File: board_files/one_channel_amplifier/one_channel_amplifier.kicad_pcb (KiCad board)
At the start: 2 copper layers, 78.7 x 33.8 mm, 27 parts, among them J1 Screw_Terminal_01x02, J2 Screw_Terminal_01x02, J3 Screw_Terminal_01x02, J4 Conn_01x02, J5 Conn_01x02, J6 Screw_Terminal_01x02, U1 LM3886

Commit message: Finished first rev
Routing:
- added copper zone on B.Cu, net GND
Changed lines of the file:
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@@
     (polygon
       (pts
-        (xy 147.32 84.582) (xy 146.304 84.963) (xy 143.256 95.25) (xy 143.256 98.806) (xy 150.114 98.806)
+        (xy 147.32 84.582) (xy 146.431 84.963) (xy 143.256 95.25) (xy 143.256 98.806) (xy 150.114 98.806)
         (xy 150.114 97.282) (xy 148.209 84.963)
-      )
-    )
-  )
-  (zone (net 2) (net_name VCC) (layer F.Cu) (hatch edge 0.508)
-    (connect_pads yes (clearance 0.508))
-    (min_thickness 0.254)
-    (fill (arc_segments 32) (thermal_gap 0.508) (thermal_bridge_width 0.508) (smoothing fillet) (radius 0.254))
-    (polygon
-      (pts
-        (xy 150.622 86.741) (xy 151.384 86.487) (xy 151.638 86.106) (xy 151.765 85.471) (xy 151.511 84.963)
-        (xy 149.86 82.042) (xy 142.24 82.042) (xy 141.859 84.963) (xy 138.938 86.106) (xy 132.842 92.202)
-        (xy 126.492 97.282) (xy 121.158 101.346) (xy 100.076 101.346) (xy 100.076 109.474) (xy 127 109.474)
-        (xy 138.176 95.758) (xy 145.034 86.868) (xy 145.796 84.328) (xy 148.844 84.328) (xy 149.733 86.233)
-        (xy 150.114 86.614)
-      )
-    )
-  )
-  (zone (net 3) (net_name VEE) (layer F.Cu) (hatch edge 0.508)
-    (priority 4)
-    (connect_pads yes (clearance 0.508))
-    (min_thickness 0.254)
-    (fill (arc_segments 32) (thermal_gap 0.508) (thermal_bridge_width 0.508) (smoothing fillet) (radius 0.254))
-    (polygon
-      (pts
-        (xy 149.987 80.01) (xy 150.114 80.518) (xy 149.987 81.026) (xy 149.606 81.407) (xy 149.098 81.661)
-        (xy 148.844 81.661) (xy 148.336 81.407) (xy 146.431 79.248) (xy 144.78 79.248) (xy 141.732 80.518)
-        (xy 138.684 80.518) (xy 135.382 81.788) (xy 131.572 81.788) (xy 121.92 84.836) (xy 100.076 84.836)
-        (xy 100.076 76.708) (xy 147.066 76.708)
       )
     )
@@
       )
     )
+  )
+  (zone (net 3) (net_name VEE) (layer F.Cu) (hatch edge 0.508)
+    (priority 4)
+    (connect_pads yes (clearance 0.508))
+    (min_thickness 0.254)
+    (fill yes (arc_segments 32) (thermal_gap 0.508) (thermal_bridge_width 0.508) (smoothing fillet) (radius 0.254))
+    (polygon
+      (pts
+        (xy 149.225 81.5975) (xy 149.6695 81.407) (xy 149.987001 81.026) (xy 150.114 80.4545) (xy 149.86 79.8195)
+        (xy 147.5105 76.7715) (xy 99.568 76.708) (xy 99.568 84.836) (xy 122.047 84.836) (xy 131.826 82.6135)
+        (xy 134.366 81.788) (xy 138.684 80.518) (xy 141.732 80.518) (xy 144.78 79.121) (xy 146.431 79.121)
+        (xy 148.1455 81.2165) (xy 148.6535 81.5975)
+      )
+    )
+  )
+  (zone (net 2) (net_name VCC) (layer F.Cu) (hatch edge 0.508)
+    (priority 4)
+    (connect_pads yes (clearance 0.508))
+    (min_thickness 0.254)
+    (fill yes (arc_segments 32) (thermal_gap 0.508) (thermal_bridge_width 0.508) (smoothing fillet) (radius 0.254))
+    (polygon
+      (pts
+        (xy 151.13 86.614) (xy 151.4475 86.4235) (xy 151.638 86.1695) (xy 151.765 85.9155) (xy 151.8285 85.5345)
+        (xy 151.5745 84.8995) (xy 150.0505 82.042) (xy 142.9385 82.042) (xy 141.7955 85.344) (xy 138.684 85.344)
+        (xy 134.3025 90.9955) (xy 131.953 92.329) (xy 121.0945 101.473) (xy 99.583875 101.473) (xy 99.552125 109.22)
+        (xy 126.90475 109.22) (xy 144.9705 86.6775) (xy 145.8595 84.201) (xy 148.844 84.201) (xy 149.6695 86.0425)
+        (xy 149.86 86.36) (xy 150.0505 86.5505) (xy 150.368 86.6775) (xy 150.6855 86.741)
+      )
+    )
+  )
+  (zone (net 10) (net_name "Net-(L1-Pad1)") (layer F.Cu) (hatch edge 0.508)
+    (priority 4)
+    (connect_pads yes (clearance 0.508))
+    (min_thickness 0.254)
+    (fill yes (arc_segments 32) (thermal_gap 0.508) (thermal_bridge_width 0.508) (smoothing fillet) (radius 0.254))
+    (polygon
+      (pts
+        (xy 147.32 84.5185) (xy 147.066 84.5185) (xy 146.7485 84.6455) (xy 146.4945 84.836) (xy 146.304 85.09)
+        (xy 146.177 85.4075) (xy 143.256 95.3135) (xy 143.256 98.806) (xy 150.114 98.806) (xy 150.114 97.282)
+        (xy 148.3995 85.471) (xy 148.2725 85.09) (xy 148.082 84.836) (xy 147.955 84.709) (xy 147.7645 84.582)
+      )
+    )
+  )
+  (zone (net 1) (net_name GND) (layer B.Cu) (hatch edge 0.508)
+    (priority 4)
+    (connect_pads yes (clearance 0.508))
+    (min_thickness 0.254)
+    (fill yes (arc_segments 32) (thermal_gap 0.508) (thermal_bridge_width 0.508) (smoothing fillet) (radius 0.254))
+    (polygon
+      (pts
+        (xy 99.568 76.708) (xy 177.292 76.835) (xy 177.292 109.601) (xy 99.568 109.22)
+      )
+    )

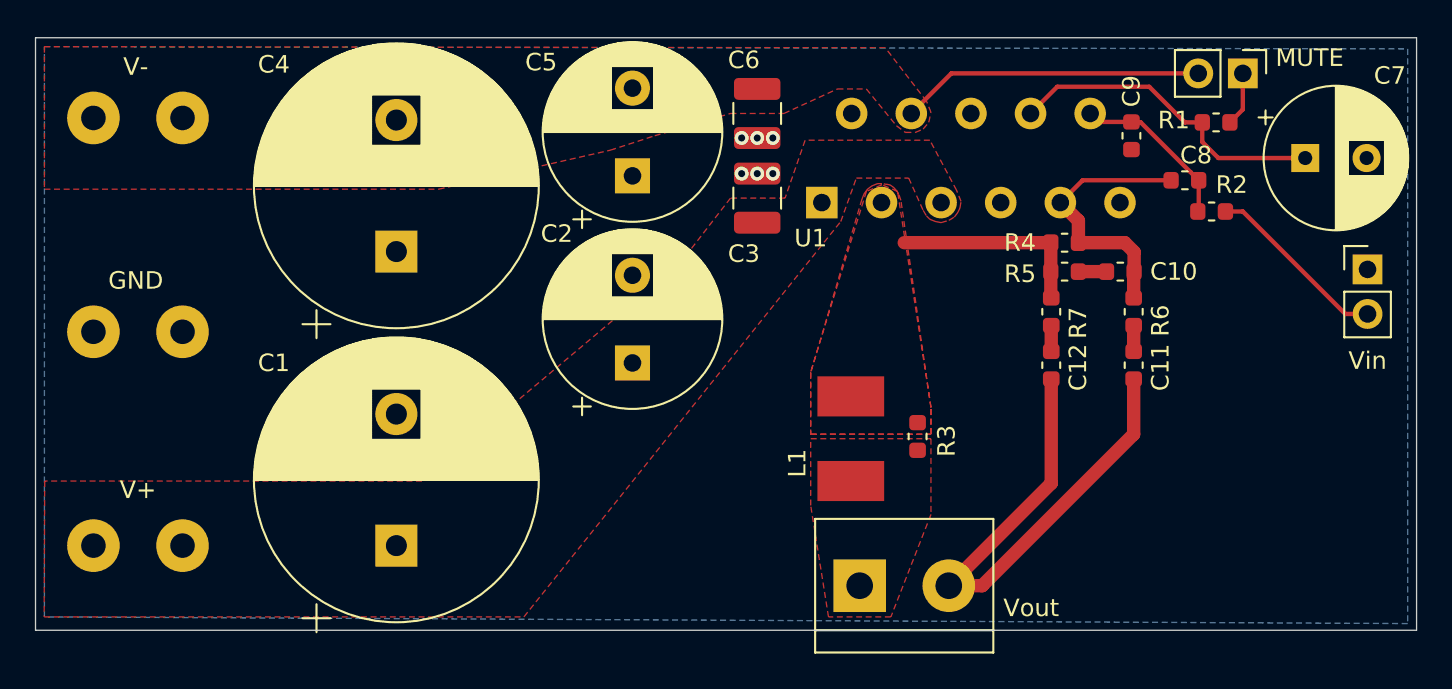
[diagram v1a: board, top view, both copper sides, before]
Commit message: Added mounting holes to amplifier PCB
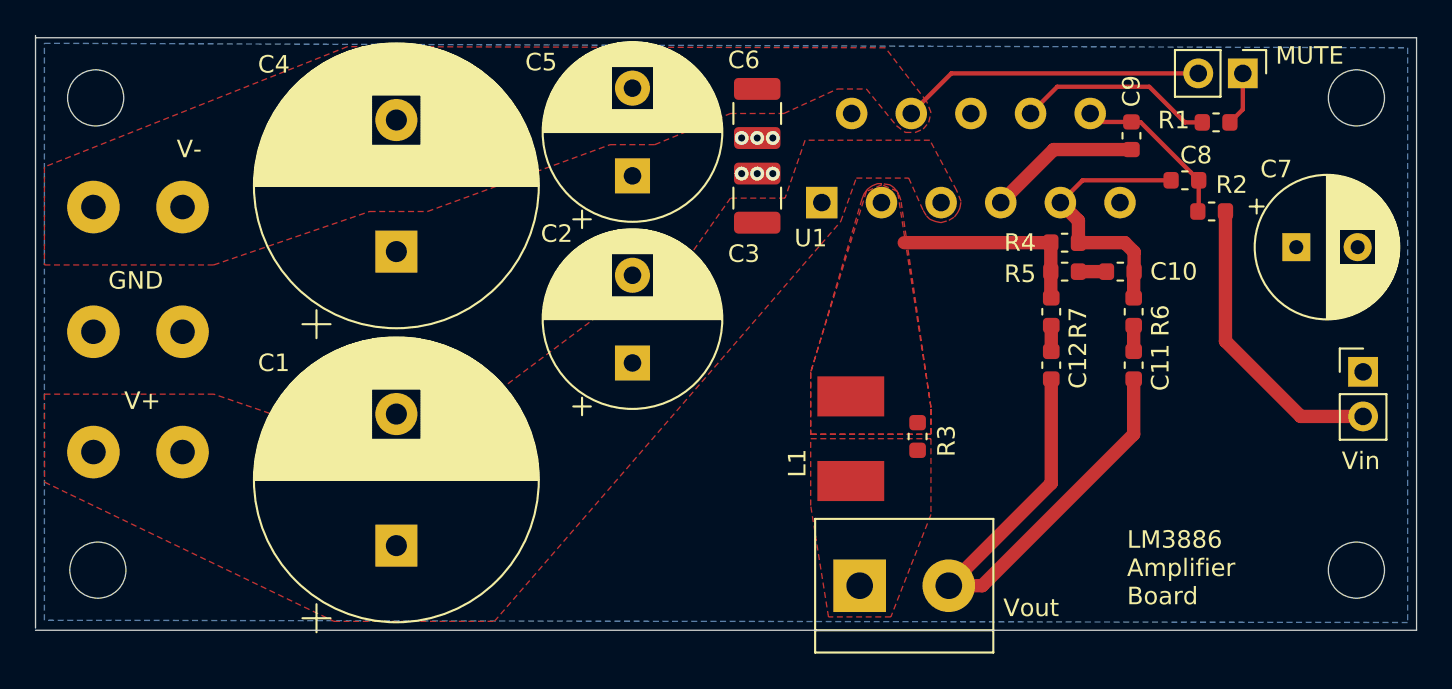
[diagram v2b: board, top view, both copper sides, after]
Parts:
- added H1: MountingHole, MountingHole:MountingHole_3.2mm_M3, F.Cu at (102.5, 79.6)
- added H2: MountingHole, MountingHole:MountingHole_3.2mm_M3, F.Cu at (174.4, 79.6)
- added H3: MountingHole, MountingHole:MountingHole_3.2mm_M3, F.Cu at (174.4, 106.6)
- added H4: MountingHole, MountingHole:MountingHole_3.2mm_M3, F.Cu at (102.6, 106.6)
- moved J5 5.85 mm to (174.8, 95.2)
- moved J1 5.33 mm to (107.4, 99.8)
- moved C7 5.11 mm to (170.9, 88.1)
- moved J3 5.08 mm to (107.4, 85.9)
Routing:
- net GND: track 31.5 -> 40.2 mm
- net Net-(C7-Pad1): track 18.6 -> 11.3 mm
- net Net-(J5-Pad2): track 10.5 -> 17.0 mm
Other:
- board size 78.7 x 33.8 mm -> 78.7 x 33.9 mm
- board text added: "LM3886 Amplifier Board"

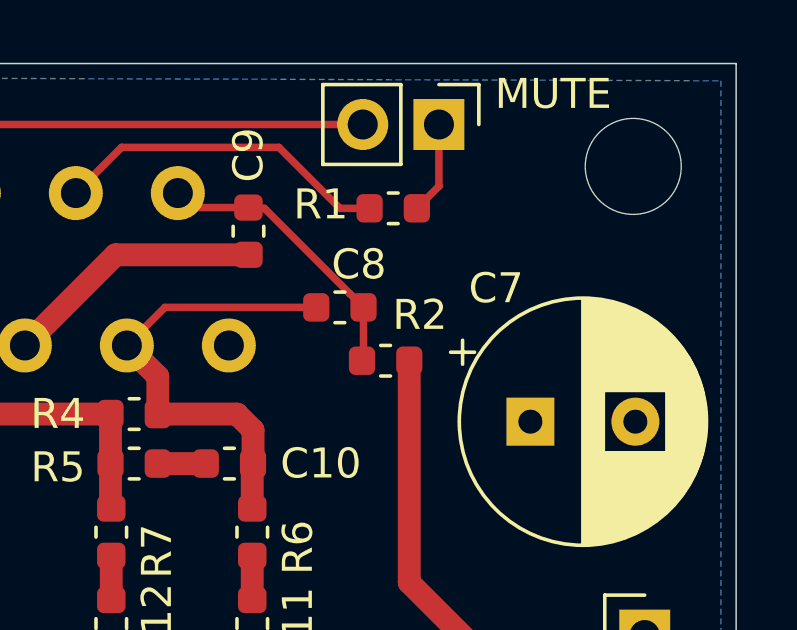
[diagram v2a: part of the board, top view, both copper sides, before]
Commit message: finished psu schematic and added front panel
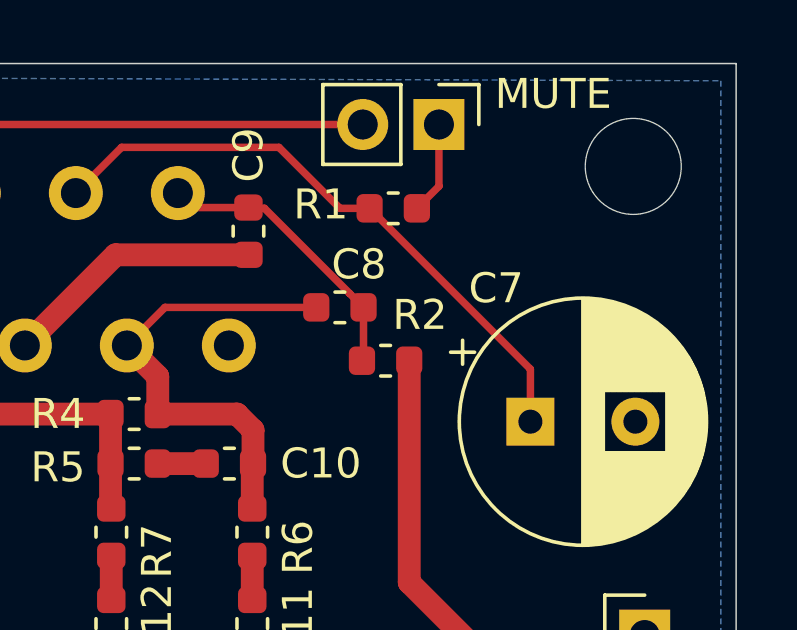
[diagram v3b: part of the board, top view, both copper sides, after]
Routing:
- net Net-(C7-Pad1): track 11.3 -> 20.6 mm
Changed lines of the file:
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@@
     (thickness 1.6)
     (drawings 13)
-    (tracks 48)
+    (tracks 50)
     (zones 0)
     (modules 31)
@@
   )
   (setup
-    (last_trace_width 0.762)
+    (last_trace_width 0.25)
     (user_trace_width 0.762)
     (trace_clearance 0.2)
@@
   (segment (start 162.56 78.994) (end 164.592 81.026) (width 0.25) (layer F.Cu) (net 4))
   (segment (start 157.315 78.994) (end 162.56 78.994) (width 0.25) (layer F.Cu) (net 4))
+  (segment (start 170.942 86.3855) (end 170.942 88.138) (width 0.25) (layer F.Cu) (net 4))
+  (segment (start 165.5825 81.026) (end 170.942 86.3855) (width 0.25) (layer F.Cu) (net 4))
   (segment (start 161.671 89.5605) (end 161.6965 89.535) (width 0.762) (layer F.Cu) (net 5))
   (segment (start 161.671 91.0335) (end 161.671 89.5605) (width 0.762) (layer F.Cu) (net 5))
